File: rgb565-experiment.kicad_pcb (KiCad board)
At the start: 4 copper layers, 101.6 x 71.1 mm, 34 parts, among them J1 ST_SHIFTER_SOCKET, J2 Conn_01x02, SW1 SW_SPDT, U1 74HC00, U2 ST_SHIFTER, U3 ST_SHIFTER, U4 74HC245, U5 74LS257, U6 74HC245

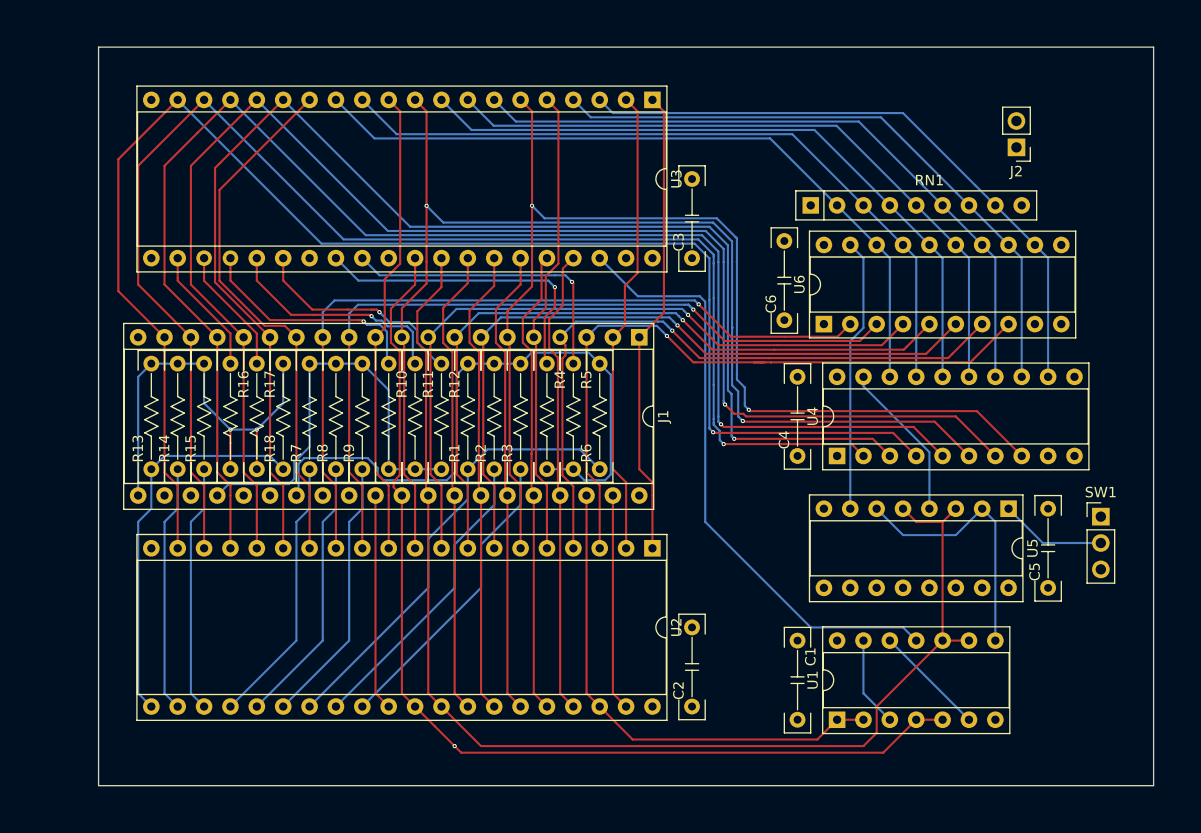
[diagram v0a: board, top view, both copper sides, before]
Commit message: copper pouring all over the faces
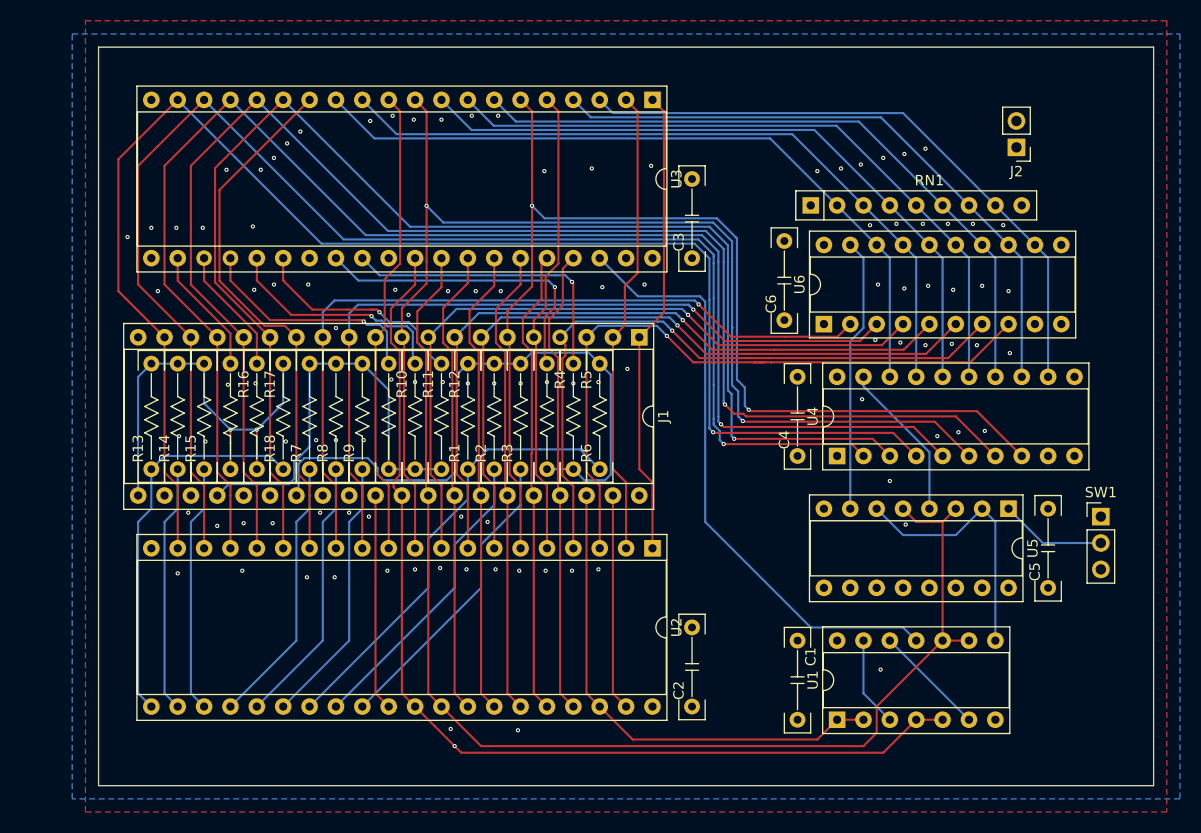
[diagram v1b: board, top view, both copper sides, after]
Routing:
- net GND: vias 0 -> 104
- added copper zone on B.Cu, net GND
- added copper zone on F.Cu, net GND

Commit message: additionnal mentions
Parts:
- added G***: LOGO, cliparts:logo--cc--zero, F.Cu at (156.8, 98.4)
- added G***: LOGO, cliparts:logo--cc--cc, F.Cu at (156.8, 104.8)
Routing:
- net /rxw: vias 1 -> 0
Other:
- board text added: "+5V – GND Additionnal Power supply"
- board text added: "0xxxx"
- board text added: "1xxxx"
- board text added: "AUXILIARY SHIFTER"
- board text added: "EXPERIMENTAL RGB-565 COLORSPACE FOR THE ATARI ST"
- board text added: "ISOLATE THIS SIDE EVERYWHERE EXCEPT THE PINS TO THE MAINBOARD SHIFTER SOCKET"
- board text added: "JLCJLCJLCJLC"
- board text added: "MAIN SHIFTER"
- board text added: "Original project : https://github.com/sporniket/atari-st-mod-rgb565-experiment"
- board text added: "Test hypothesis : palette registers address range"
- board text added: "WITHOUT ANY WARRANTY OF ANY KIND, INCLUDING, BUT NOT LIMITED TO, THE IMPLIED WARRANTIES OF SAFETY, MERCHANTABILITY AND FITNESS FOR A PARTICULAR PURPOSE."

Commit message: version 1 experience candidate 1
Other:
- board text added: "Original project : https://github.com/sporniket/atari-st-mod-rgb565-experiment v1.0.0-xprc1"
- board text removed: "Original project : https://github.com/sporniket/atari-st-mod-rgb565-experiment"
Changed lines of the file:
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@@
   )
   (page A4)
+  (title_block
+    (title "Experimental RGB-565 mod for the Atari ST")
+    (date 2021-12-18)
+    (rev v1.0.0-xprc1)
+    (company Sporniket-Studio.com)
+  )
   (layers
     (0 F.Cu signal)
@@
     (effects (font (size 1 1) (thickness 0.15)) (justify mirror))
   )
-  (gr_text "Original project : https://github.com/sporniket/atari-st-mod-rgb565-experiment" (at 133.35 133.35) (layer F.SilkS)
+  (gr_text "Original project : https://github.com/sporniket/atari-st-mod-rgb565-experiment v1.0.0-xprc1" (at 139.7 133.35) (layer F.SilkS)
     (effects (font (size 1 1) (thickness 0.15)))
   )

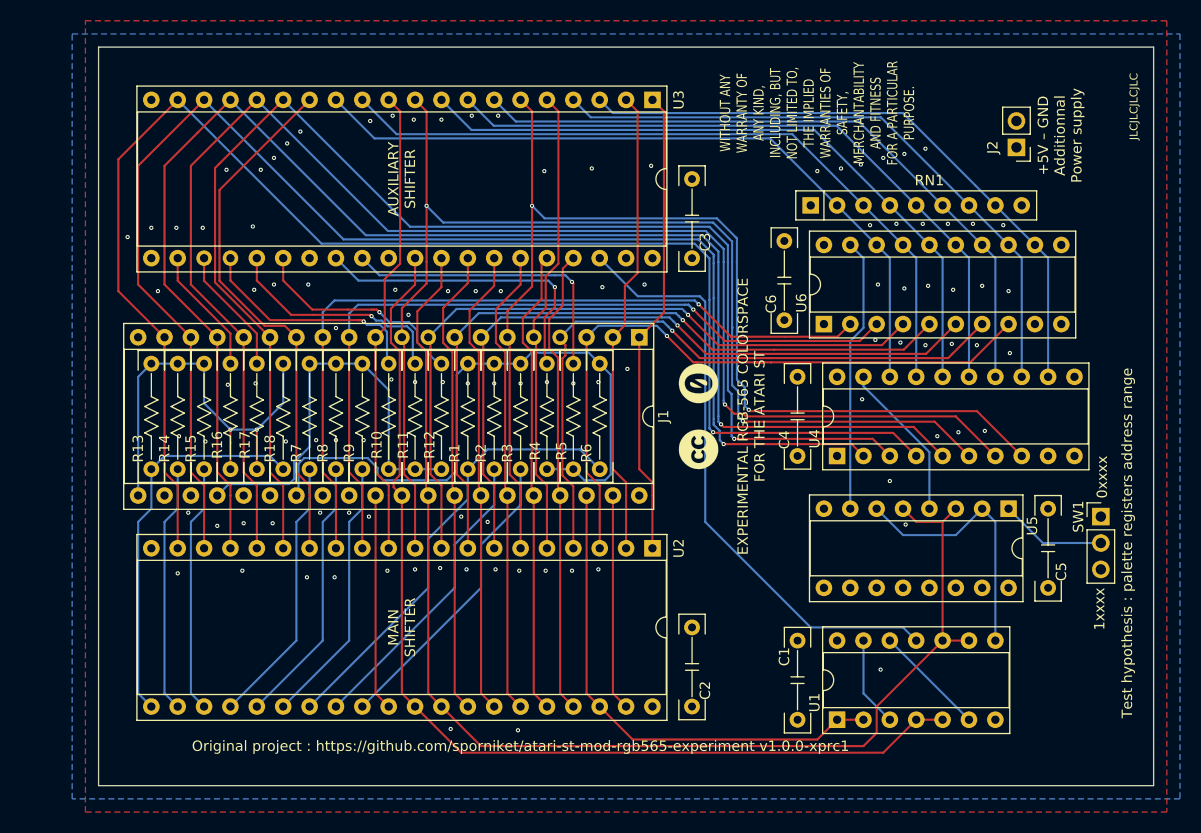
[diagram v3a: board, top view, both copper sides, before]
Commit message: Adjust width to be a bit narrower
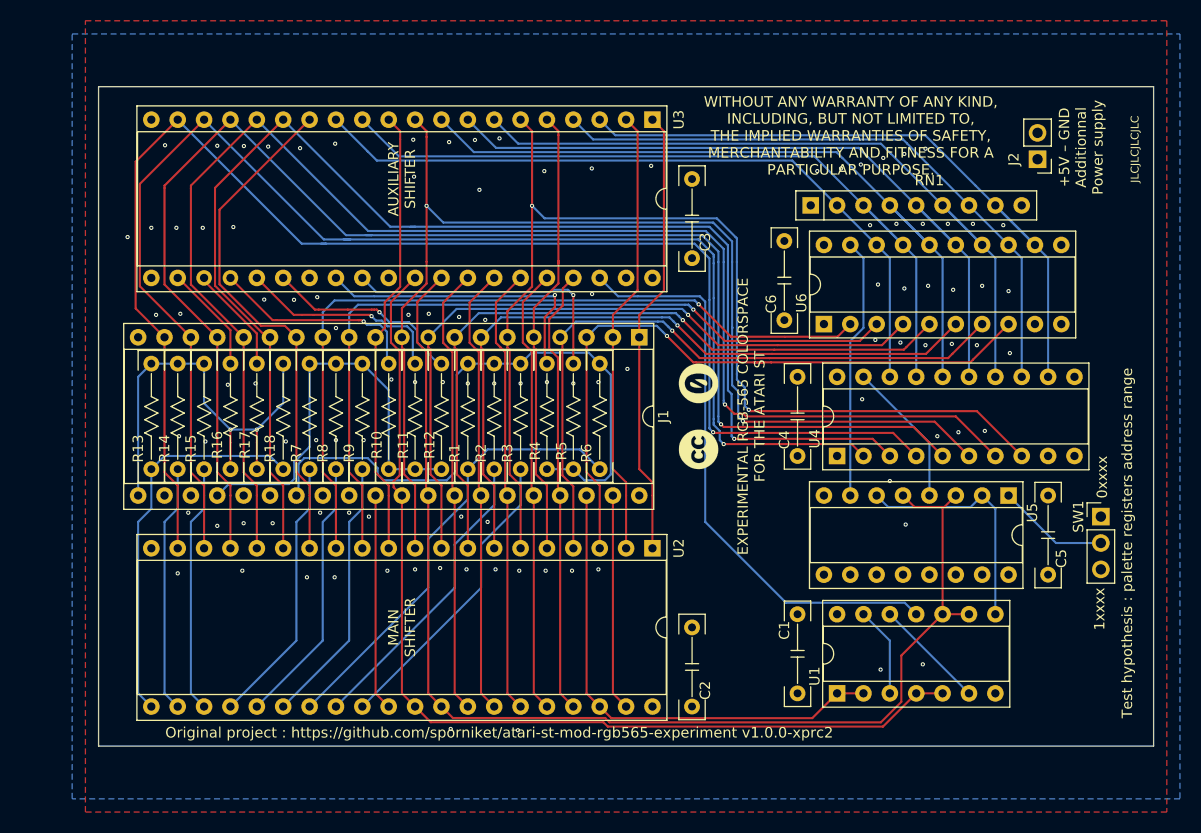
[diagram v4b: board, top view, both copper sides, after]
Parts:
- moved C1 2.54 mm to (166.4, 124.5)
- moved U1 2.54 mm to (170.2, 128.3)
- moved J2 2.33 mm to (189.5, 76.8)
- moved U3 1.91 mm to (152.4, 73.0)
- moved C5 1.27 mm to (190.5, 113.0)
- moved U5 1.27 mm to (186.7, 109.2)
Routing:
- net /DAT8: track 71.1 -> 75.7 mm
- net /DAT0: track 60.9 -> 65.5 mm
- net /DAT6: track 66.0 -> 70.6 mm
- net /DAT5: track 66.0 -> 70.6 mm
- net /DAT4: track 66.0 -> 70.6 mm
- net /d15: track 142.8 -> 139.2 mm
- net /rxw: track 99.5 -> 96.6 mm
- net /a5: track 120.7 -> 117.9 mm
- net Net-(U1-Pad8): track 25.5 -> 23.0 mm
- net /d14: track 136.3 -> 134.1 mm
- net /d13: track 140.8 -> 138.7 mm
- net /g2: track 22.7 -> 20.6 mm
- net /g0: track 21.4 -> 19.3 mm
- net /g1: track 22.4 -> 20.3 mm
- net /d11: track 131.8 -> 129.8 mm
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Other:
- board size 101.6 x 71.1 mm -> 101.6 x 63.5 mm
- board text added: "Original project : https://github.com/sporniket/atari-st-mod-rgb565-experiment v1.0.0-xprc2"
- board text removed: "Original project : https://github.com/sporniket/atari-st-mod-rgb565-experiment v1.0.0-xprc1"

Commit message: shaving a little bit of length beside shifter sockets
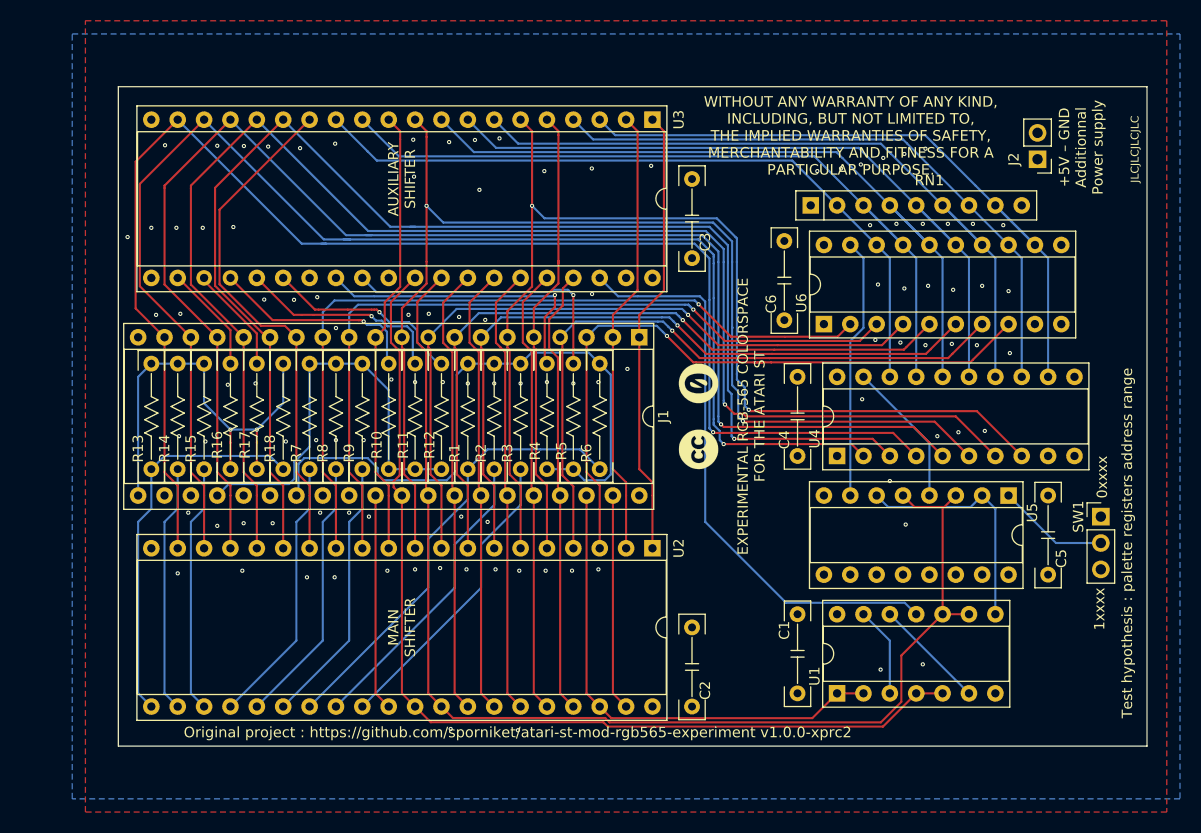
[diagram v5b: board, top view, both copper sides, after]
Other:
- board size 101.6 x 63.5 mm -> 99.1 x 63.5 mm
